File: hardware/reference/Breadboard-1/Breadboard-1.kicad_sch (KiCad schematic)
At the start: 62 parts, among them J1 Left, J2 Right, J3 ICSP, J4 TTL Serial, Q31 HSM0903, Q32 HSM0903, Q33 DTC143ZE, Q34 DTC143ZE, Q41 2N7002, Q42 2N7002, Q43 2N7002, U11 AMS1117-5.0, U21 PIC18F06Q40-x/SS

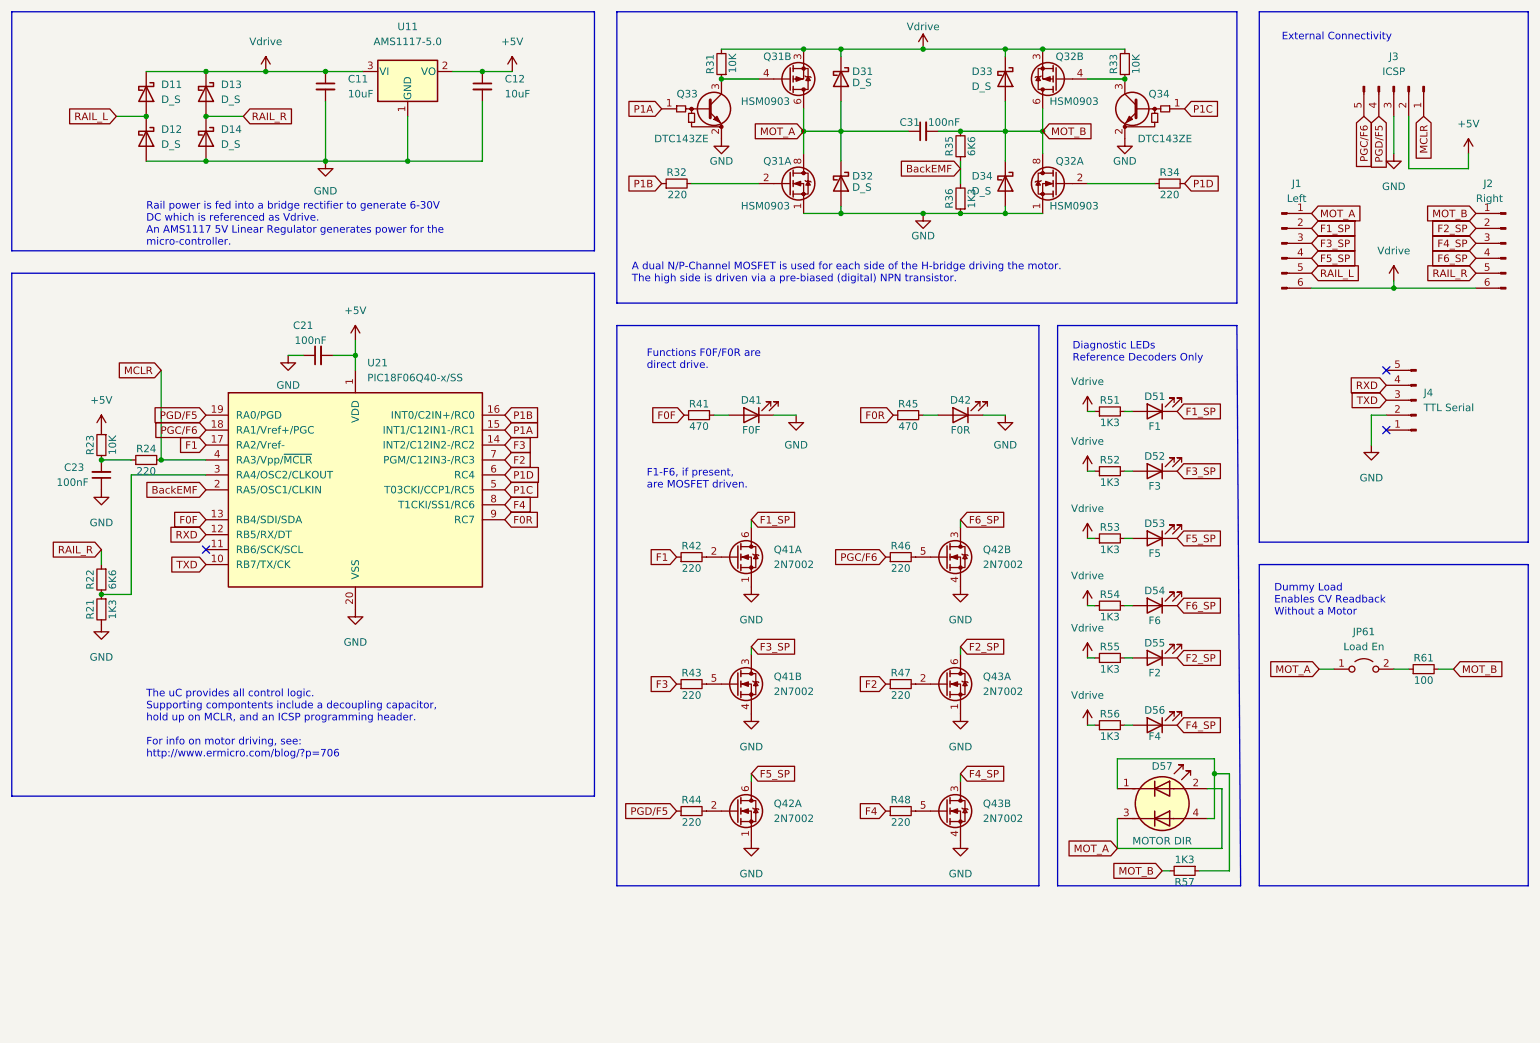
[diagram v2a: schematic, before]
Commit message: Attempt to refactor with all SOT-23 components for cost, availability.
Also makes it more possible to hand-solder.
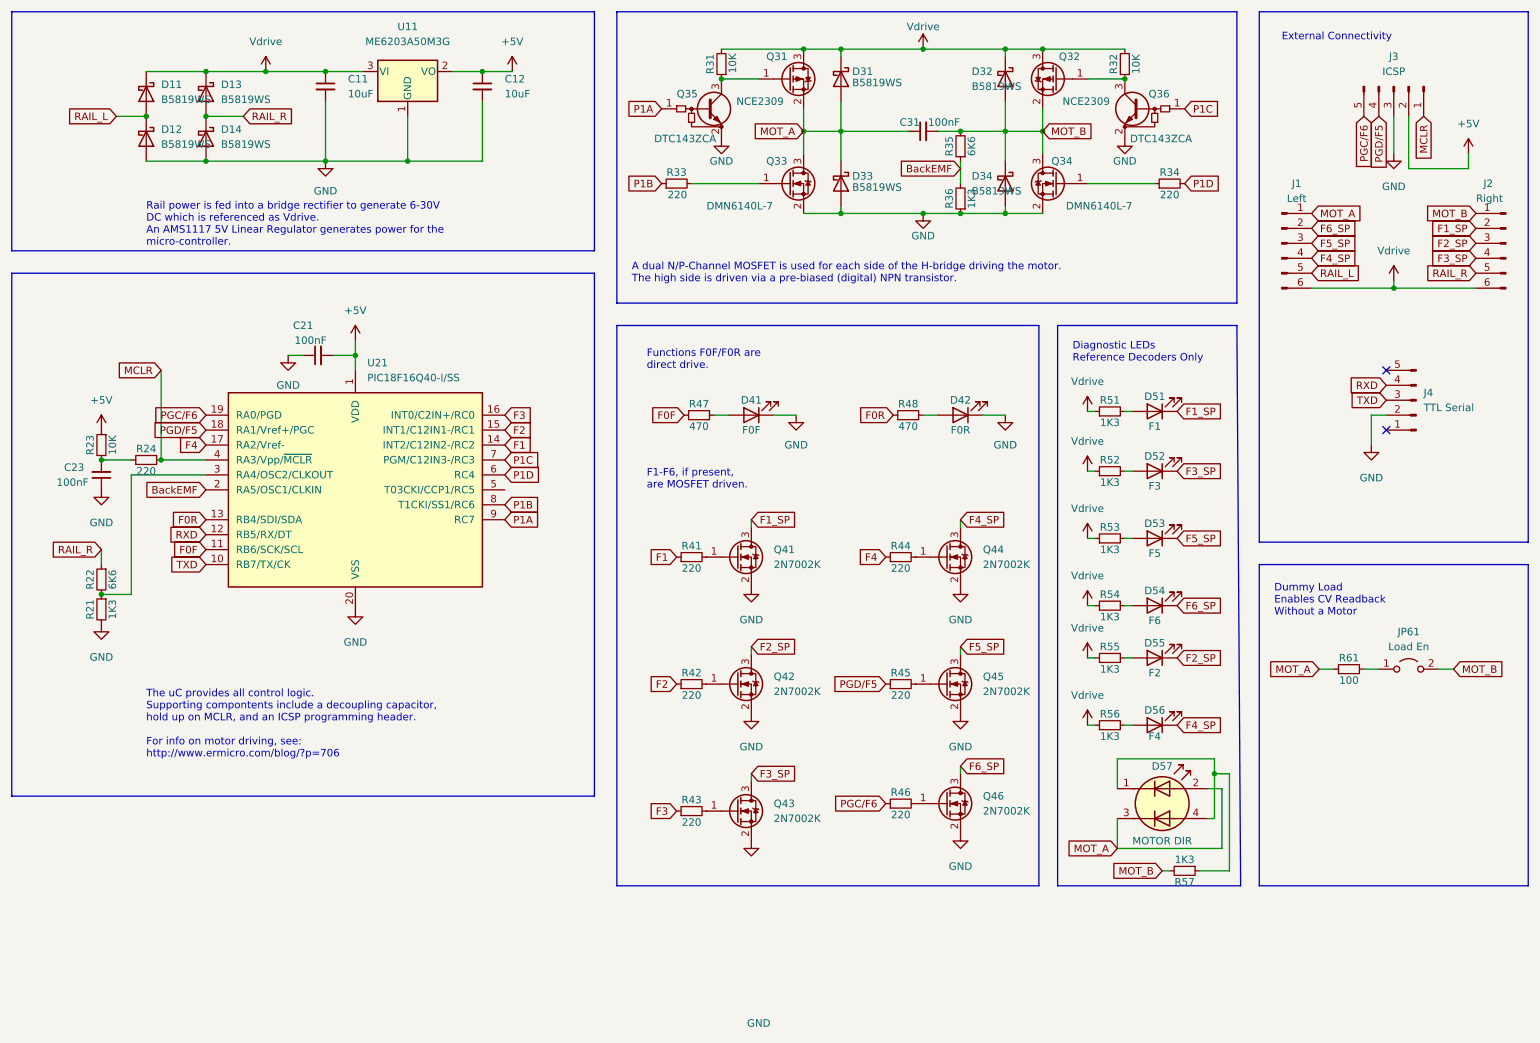
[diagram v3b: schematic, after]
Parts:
- removed Q31, Q32: HSM0903, Package_SO:SOP-8_3.9x4.9mm_P1.27mm, symbol Leo's Library:TPC8408
- removed Q41, Q42, Q43: 2N7002, Package_TO_SOT_SMD:SOT-363_SC-70-6, symbol Transistor_FET:FDG1024NZ
- added Q31, Q32: NCE2309, Package_TO_SOT_SMD:SOT-23, symbol Transistor_FET:AO3401A
- added Q33, Q34: DMN6140L-7, Package_TO_SOT_SMD:SOT-23, symbol Transistor_FET:2N7002K
- added Q41, Q42, Q43, Q44, Q45, Q46: 2N7002K, Package_TO_SOT_SMD:SOT-23, symbol Transistor_FET:2N7002K
- C11, C12: Cost (none) -> 0.10
- C21, C23, C31: footprint Capacitor_SMD:C_0402_1005Metric -> Capacitor_SMD:C_0805_2012Metric; Cost (none) -> 0.01; Specification 0402 50V 100nF X7R 10% -> 0805 50V 100nF X7R 10%
- D11, D12, D13, D14, D31, D34: value D_S -> B5819WS; footprint Diode_SMD:D_SOD-523 -> Diode_SMD:D_SOD-323; Cost (none) -> 0.01; Specification SOD-523, 50V, 1A Schottky barrier rectifier diode -> SOD-323, 40V, 1A Schottky barrier rectifier diode
- D32: renamed from D33; value D_S -> B5819WS; footprint Diode_SMD:D_SOD-523 -> Diode_SMD:D_SOD-323; Cost (none) -> 0.01; Specification SOD-523, 50V, 1A Schottky barrier rectifier diode -> SOD-323, 40V, 1A Schottky barrier rectifier diode
- D33: renamed from D32; value D_S -> B5819WS; footprint Diode_SMD:D_SOD-523 -> Diode_SMD:D_SOD-323; Cost (none) -> 0.01; Specification SOD-523, 50V, 1A Schottky barrier rectifier diode -> SOD-323, 40V, 1A Schottky barrier rectifier diode
- D41, D42, D51, D52, D53, D54, D55, D56, J1, J2: Cost (none) -> 0.02
- D57: Cost (none) -> 0.02; Specification (none) -> 1210 RG LED, 20ma, Vf 1.95v
- J3: Cost (none) -> 0.03; Specification 5 position 2.54mm pin header -> 5 position 2.54mm pin header - right angle
- J4: Cost (none) -> 0.02; Specification 5 position 2.54mm pin header -> 5 position 2.54mm pin socket
- JP61: Cost (none) -> 0.01; Specification (none) -> 2 position 2.54mm pin header
- Q35: renamed from Q33; value DTC143ZE -> DTC143ZCA; footprint Package_TO_SOT_SMD:SOT-523 -> Package_TO_SOT_SMD:SOT-23; Cost (none) -> 0.02; Specification (none) -> SOT-23 50V 100ma NPN - Pre Biased 4.7K/47K
- Q36: renamed from Q34; value DTC143ZE -> DTC143ZCA; footprint Package_TO_SOT_SMD:SOT-523 -> Package_TO_SOT_SMD:SOT-23; Cost (none) -> 0.02; Specification (none) -> SOT-23 50V 100ma NPN - Pre Biased 4.7K/47K
- R21, R36, R51, R52, R53, R54, R55, R56, R57: footprint Resistor_SMD:R_0402_1005Metric -> Resistor_SMD:R_0805_2012Metric; Cost (none) -> 0.01; Specification 0402 1.33K Ω 1% 1/8W -> 0805 1.33K Ω 1% 1/8W
- R22, R35: footprint Resistor_SMD:R_0402_1005Metric -> Resistor_SMD:R_0805_2012Metric; Cost (none) -> 0.01; Specification 0402 6.65K Ω 1% 1/8W -> 0805 6.65K Ω 1% 1/8W
- R23, R31: footprint Resistor_SMD:R_0402_1005Metric -> Resistor_SMD:R_0805_2012Metric; Cost (none) -> 0.01; Specification 0402 10K Ω 1% 1/8W -> 0805 10K Ω 1% 1/8W
- R24, R34, R43, R46: footprint Resistor_SMD:R_0402_1005Metric -> Resistor_SMD:R_0805_2012Metric; Cost (none) -> 0.01; Specification 0402 220 Ω 1% 1/8W -> 0805 220 Ω 1% 1/8W
- R32: renamed from R33; footprint Resistor_SMD:R_0402_1005Metric -> Resistor_SMD:R_0805_2012Metric; Cost (none) -> 0.01; Specification 0402 10K Ω 1% 1/8W -> 0805 10K Ω 1% 1/8W
- R33: renamed from R32; footprint Resistor_SMD:R_0402_1005Metric -> Resistor_SMD:R_0805_2012Metric; Cost (none) -> 0.01; Specification 0402 220 Ω 1% 1/8W -> 0805 220 Ω 1% 1/8W
- R41: renamed from R42; footprint Resistor_SMD:R_0402_1005Metric -> Resistor_SMD:R_0805_2012Metric; Cost (none) -> 0.01; Specification 0402 220 Ω 1% 1/8W -> 0805 220 Ω 1% 1/8W
- R42: renamed from R47; footprint Resistor_SMD:R_0402_1005Metric -> Resistor_SMD:R_0805_2012Metric; Cost (none) -> 0.01; Specification 0402 220 Ω 1% 1/8W -> 0805 220 Ω 1% 1/8W
- R44: renamed from R48; footprint Resistor_SMD:R_0402_1005Metric -> Resistor_SMD:R_0805_2012Metric; Cost (none) -> 0.01; Specification 0402 220 Ω 1% 1/8W -> 0805 220 Ω 1% 1/8W
- R45: renamed from R44; footprint Resistor_SMD:R_0402_1005Metric -> Resistor_SMD:R_0805_2012Metric; Cost (none) -> 0.01; Specification 0402 220 Ω 1% 1/8W -> 0805 220 Ω 1% 1/8W
- R47: renamed from R41; footprint Resistor_SMD:R_0402_1005Metric -> Resistor_SMD:R_0805_2012Metric; Cost (none) -> 0.01; Specification 0402 470 Ω 1% 1/8W -> 0805 470 Ω 1% 1/8W
- R48: renamed from R45; footprint Resistor_SMD:R_0402_1005Metric -> Resistor_SMD:R_0805_2012Metric; Cost (none) -> 0.01; Specification 0402 470 Ω 1% 1/8W -> 0805 470 Ω 1% 1/8W
- R61: Cost (none) -> 0.01
- U11: value AMS1117-5.0 -> ME6203A50M3G; footprint Package_TO_SOT_SMD:SOT-223-3_TabPin2 -> Package_TO_SOT_SMD:SOT-23; Cost (none) -> 0.08; Specification 5V Linear Regulator -> SOT-23 180ma 40V to 5V LDO
- U21: value PIC18F06Q40-x/SS -> PIC18F16Q40-I/SS; Cost (none) -> 1.50
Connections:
- net F0F: now also U21.11 (RB6/SCK/SCL); no longer U21.13 (RB4/SDI/SDA)
- net F0R: now also U21.13 (RB4/SDI/SDA); no longer U21.9 (RC7)
- net F1: now also U21.14 (INT2/C12IN2-/RC2); no longer U21.17 (RA2/Vref-)
- net F1_SP: now also J2.2 (Pin_2), Q41.3 (D); no longer J1.2 (Pin_2)
- net F2: now also U21.15 (INT1/C12IN1-/RC1); no longer U21.7 (PGM/C12IN3-/RC3)
- net F2_SP: now also J2.3 (Pin_3), Q42.3 (D); no longer J2.2 (Pin_2)
- net F3: now also U21.16 (INT0/C2IN+/RC0); no longer U21.14 (INT2/C12IN2-/RC2)
- net F3_SP: now also J2.4 (Pin_4), Q43.3 (D); no longer J1.3 (Pin_3)
- net F4: now also U21.17 (RA2/Vref-); no longer U21.8 (T1CKI/SS1/RC6)
- net F4_SP: now also J1.4 (Pin_4), Q44.3 (D); no longer J2.3 (Pin_3)
- net F5_SP: now also J1.3 (Pin_3), Q45.3 (D); no longer J1.4 (Pin_4)
- net F6_SP: now also J1.2 (Pin_2), Q46.3 (D); no longer J2.4 (Pin_4)
- net GND: now also Q33.2 (S), Q34.2 (S), Q41.2 (S), Q42.2 (S), Q43.2 (S), Q44.2 (S), Q45.2 (S), Q46.2 (S)
- net MOT_A: now also R61.1, Q31.2 (S), Q33.3 (D); no longer JP61.1 (A)
- net MOT_B: now also JP61.2 (B), Q32.2 (S), Q34.3 (D); no longer R61.2
- net P1A: now also U21.9 (RC7); no longer U21.15 (INT1/C12IN1-/RC1)
- net P1B: now also U21.8 (T1CKI/SS1/RC6); no longer U21.16 (INT0/C2IN+/RC0)
- net P1C: now also U21.7 (PGM/C12IN3-/RC3); no longer U21.5 (T03CKI/CCP1/RC5)
- net PGC/F6: now also U21.19 (RA0/PGD); no longer U21.18 (RA1/Vref+/PGC)
- net PGD/F5: now also U21.18 (RA1/Vref+/PGC); no longer U21.19 (RA0/PGD)
- net Vdrive: now also Q31.3 (D), Q32.3 (D)
- net at Q36.3 (C), R32.1: now also Q32.1 (G)
- net at R44.2: now also Q44.1 (G)
- net at R42.2: now also Q42.1 (G)
- net at R43.2: now also Q43.1 (G)
- net at R46.2: now also Q46.1 (G)
- net at R45.2: now also Q45.1 (G)
- net at Q35.3 (C), R31.1: now also Q31.1 (G)
- net at R33.2: now also Q33.1 (G)
- net at R34.1: now also Q34.1 (G)
- net at R41.2: now also Q41.1 (G)
- new net: JP61.1 (A), R61.2
- no-connect marks 3 -> 2
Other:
- moved on the sheet: JP61, R42, R43, R44, R45, R46, R61

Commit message: Cleanup of the final PCB.
Moved components to grid coordinates.
Added in some labels for the user.
Cleaned up some trace routing, and made it pretty where possible.
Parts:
- removed D31, D32, D33, D34: B5819WS, Diode_SMD:D_SOD-323, symbol Device:D_Schottky
- added C32: 1uF, Capacitor_SMD:C_0805_2012Metric, symbol Device:C_Small
- added J4: Oscilloscope, Connector_PinHeader_2.54mm:PinHeader_1x07_P2.54mm_Vertical, symbol Connector:Conn_01x07_Male
- added R36: 6K6, Resistor_SMD:R_0805_2012Metric, symbol Device:R_Small
- J5: renamed from J4; footprint Connector_PinSocket_2.54mm:PinSocket_1x05_P2.54mm_Vertical -> Connector_PinSocket_2.54mm:PinSocket_1x05_P2.54mm_Horizontal
- renumbered R36 to R37
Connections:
- net BackEMF: now also J4.5 (Pin_5), R36.1
- net GND: now also C31.1, J5.4 (Pin_4), C32.1, J4.7 (Pin_7); no longer J5.2 (Pin_2)
- net MOT_A: now also R35.2; no longer C31.1
- net MOT_B: now also R36.2; no longer C31.2, R35.2
- net P1A: now also J4.1 (Pin_1)
- net P1B: now also J4.2 (Pin_2)
- net P1C: now also J4.3 (Pin_3)
- net P1D: now also J4.4 (Pin_4)
- net RXD: now also J5.2 (Pin_2); no longer J5.4 (Pin_4)
- net Vdrive: now also C31.2, C32.2
- net DCC_IN: now reaches R21.1, R22.2, U21.3 (RA4/OSC2/CLKOUT)
- net DCC_IN: now also J4.6 (Pin_6)
- no-connect marks 2 -> 3
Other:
- note added: "A dual N/P-Channel MOSFET is used for each side of the H-bridge driving the motor. The high side is driven via a pre-biased (digital) NPN transistor. A trio of resistors create a single BackEMF measurement independent of motor direction."
- note removed: "A dual N/P-Channel MOSFET is used for each side of the H-bridge driving the motor. The high side is driven via a pre-biased (digital) NPN transistor."
- moved on the sheet: C23, C31, J5, R21, R22, R23, R24, R35, R37

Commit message: Minor design tweak, update documentation.
Moved the MCLEAR hold up components to make the board design cleaner.

Updated all the documentation to match the current configuration.
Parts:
- J3: Cost 0.03 -> 0.02
- J4: Cost (none) -> 0.02; Specification (none) -> 7 position 2.54mm pin header
- J5: Specification 5 position 2.54mm pin socket -> 5 position 2.54mm pin socket - right angle
- JP61: Cost 0.01 -> 0.02
- R61: Cost 0.01 -> 0.12
- U21: Specification (none) -> PIC18F16Q40-I/SS, PIC18F16Q40T-I/SS, PIC18F16Q40-E/SS
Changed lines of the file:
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@@
   (junction (at 73.66 73.66) (diameter 0) (color 0 0 0 0)
   )
+  (junction (at 154.94 35.56) (diameter 0) (color 0 0 0 0)
+  )
   (junction (at 27.94 114.3) (diameter 0) (color 0 0 0 0)
   )
@@
   )
   (junction (at 68.58 40.64) (diameter 0) (color 0 0 0 0)
+  )
+  (junction (at 185.42 35.56) (diameter 0) (color 0 0 0 0)
   )
   (junction (at 48.26 25.4) (diameter 0) (color 0 0 0 0)
@@
     (stroke (width 0) (type default) (color 0 0 0 0))
   )
+  (wire (pts (xy 154.94 35.56) (xy 160.02 35.56))
+    (stroke (width 0) (type default) (color 0 0 0 0))
+  )
   (wire (pts (xy 219.71 142.24) (xy 219.71 144.78))
     (stroke (width 0) (type default) (color 0 0 0 0))
@@
   )
   (wire (pts (xy 165.1 26.67) (xy 165.1 29.21))
+    (stroke (width 0) (type default) (color 0 0 0 0))
+  )
+  (wire (pts (xy 180.34 35.56) (xy 185.42 35.56))
     (stroke (width 0) (type default) (color 0 0 0 0))
   )
@@
     )
   )
-  (global_label "MOT_B" (shape input) (at 190.5 35.56 0) (fields_autoplaced)
-    (effects (font (size 1.27 1.27)) (justify left))
-    (property "Intersheet References" "${INTERSHEET_REFS}" (id 0) (at 198.9002 35.4806 0)
-      (effects (font (size 1.27 1.27)) (justify left) hide)
+  (global_label "MOT_B" (shape input) (at 180.34 35.56 180) (fields_autoplaced)
+    (effects (font (size 1.27 1.27)) (justify right))
+    (property "Intersheet References" "${INTERSHEET_REFS}" (id 0) (at 171.9398 35.6394 0)
+      (effects (font (size 1.27 1.27)) (justify right) hide)
     )
   )
@@
     )
   )
-  (global_label "MOT_A" (shape input) (at 149.86 35.56 180) (fields_autoplaced)
-    (effects (font (size 1.27 1.27)) (justify right))
-    (property "Intersheet References" "${INTERSHEET_REFS}" (id 0) (at 141.6412 35.4806 0)
-      (effects (font (size 1.27 1.27)) (justify right) hide)
+  (global_label "MOT_A" (shape input) (at 160.02 35.56 0) (fields_autoplaced)
+    (effects (font (size 1.27 1.27)) (justify left))
+    (property "Intersheet References" "${INTERSHEET_REFS}" (id 0) (at 168.2388 35.6394 0)
+      (effects (font (size 1.27 1.27)) (justify left) hide)
     )
   )
@@
       (effects (font (size 1.27 1.27)) hide)
     )
-    (property "Cost" "0.01" (id 5) (at 242.57 127 0)
+    (property "Cost" "0.12" (id 5) (at 242.57 127 0)
       (effects (font (size 1.27 1.27)) hide)
     )
@@
     )
     (property "Cost" "1.50" (id 4) (at 73.66 96.52 0)
+      (effects (font (size 1.27 1.27)) hide)
+    )
+    (property "Specification" "PIC18F16Q40-I/SS, PIC18F16Q40T-I/SS, PIC18F16Q40-E/SS" (id 5) (at 73.66 96.52 0)
       (effects (font (size 1.27 1.27)) hide)
     )
@@
       (effects (font (size 1.27 1.27)) hide)
     )
-    (property "Cost" "0.01" (id 5) (at 252.73 127 0)
+    (property "Cost" "0.02" (id 5) (at 252.73 127 0)
       (effects (font (size 1.27 1.27)) hide)
     )
@@
       (effects (font (size 1.27 1.27)) hide)
     )
-    (property "Specification" "5 position 2.54mm pin socket" (id 4) (at 267.97 78.74 0)
+    (property "Specification" "5 position 2.54mm pin socket - right angle" (id 4) (at 267.97 78.74 0)
       (effects (font (size 1.27 1.27)) hide)
     )
@@
       (effects (font (size 1.27 1.27)) hide)
     )
-    (property "Datasheet" "~" (id 3) (at 231.14 81.28 0)
+    (property "Datasheet" "Generic Passive" (id 3) (at 231.14 81.28 0)
+      (effects (font (size 1.27 1.27)) hide)
+    )
+    (property "Cost" "0.02" (id 4) (at 231.14 81.28 0)
+      (effects (font (size 1.27 1.27)) hide)
+    )
+    (property "Specification" "7 position 2.54mm pin header" (id 5) (at 231.14 81.28 0)
       (effects (font (size 1.27 1.27)) hide)
     )
@@
       (effects (font (size 1.27 1.27)) hide)
     )
-    (property "Cost" "0.03" (id 5) (at 250.19 27.94 0)
-      (effects (font (size 1.27 1.27)) hide)
-    )
+    (property "Cost" "0.02" (id 5) (at 250.19 27.94 0)
+      (effects (font (size 1.27 1.27)) hide)
+    )

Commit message: Manufacturability changes.
Added 3 fiducial markers to support pick and place in volume.
Resized all the traces to be manufacturable with the popular board fabs.
Moved traces based on the new size.
Standardized vias to one size larger than the general manufacturing minimum.
Improved grounding around the CPU.
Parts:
- added FID1, FID2, FID3: Fiducial, Fiducial:Fiducial_0.75mm_Mask2.25mm, symbol Mechanical:Fiducial
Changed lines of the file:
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@@
     (pin "3")
+  )
+  (symbol (lib_id "Mechanical:Fiducial") (at 101.6 132.08 0) (unit 1)
+    (in_bom yes) (on_board yes) (fields_autoplaced)
+    (property "Reference" "FID3" (id 0) (at 104.14 130.8099 0)
+      (effects (font (size 1.27 1.27)) (justify left))
+    )
+    (property "Value" "Fiducial" (id 1) (at 104.14 133.3499 0)
+      (effects (font (size 1.27 1.27)) (justify left))
+    )
+    (property "Footprint" "Fiducial:Fiducial_0.75mm_Mask2.25mm" (id 2) (at 101.6 132.08 0)
+      (effects (font (size 1.27 1.27)) hide)
+    )
+    (property "Datasheet" "~" (id 3) (at 101.6 132.08 0)
+      (effects (font (size 1.27 1.27)) hide)
+    )
   )
   (symbol (lib_id "power:Vdrive") (at 198.12 104.775 0) (unit 1)
@@
     (pin "2")
   )
+  (symbol (lib_id "Mechanical:Fiducial") (at 101.6 125.73 0) (unit 1)
+    (in_bom yes) (on_board yes) (fields_autoplaced)
+    (property "Reference" "FID2" (id 0) (at 104.14 124.4599 0)
+      (effects (font (size 1.27 1.27)) (justify left))
+    )
+    (property "Value" "Fiducial" (id 1) (at 104.14 126.9999 0)
+      (effects (font (size 1.27 1.27)) (justify left))
+    )
+    (property "Footprint" "Fiducial:Fiducial_0.75mm_Mask2.25mm" (id 2) (at 101.6 125.73 0)
+      (effects (font (size 1.27 1.27)) hide)
+    )
+    (property "Datasheet" "~" (id 3) (at 101.6 125.73 0)
+      (effects (font (size 1.27 1.27)) hide)
+    )
+  )
   (symbol (lib_id "power:GND") (at 170.18 29.21 0) (unit 1)
     (in_bom yes) (on_board yes)
@@
     (pin "2")
     (pin "3")
+  )
+  (symbol (lib_id "Mechanical:Fiducial") (at 101.6 119.38 0) (unit 1)
+    (in_bom yes) (on_board yes) (fields_autoplaced)
+    (property "Reference" "FID1" (id 0) (at 104.14 118.1099 0)
+      (effects (font (size 1.27 1.27)) (justify left))
+    )
+    (property "Value" "Fiducial" (id 1) (at 104.14 120.6499 0)
+      (effects (font (size 1.27 1.27)) (justify left))
+    )
+    (property "Footprint" "Fiducial:Fiducial_0.75mm_Mask2.25mm" (id 2) (at 101.6 119.38 0)
+      (effects (font (size 1.27 1.27)) hide)
+    )
+    (property "Datasheet" "~" (id 3) (at 101.6 119.38 0)
+      (effects (font (size 1.27 1.27)) hide)
+    )
   )
   (symbol (lib_id "power:+5V") (at 100.33 25.4 0) (unit 1)
@@
       (reference "D57") (unit 1) (value "MOTOR DIR") (footprint "LED_SMD:LED_RGB_1210")
     )
+    (path "/b1e3d7d1-5e1a-4783-b95d-60ad9975723b"
+      (reference "FID1") (unit 1) (value "Fiducial") (footprint "Fiducial:Fiducial_0.75mm_Mask2.25mm")
+    )
+    (path "/89d0e1b6-392a-4bac-b2c2-159e11a37d08"
+      (reference "FID2") (unit 1) (value "Fiducial") (footprint "Fiducial:Fiducial_0.75mm_Mask2.25mm")
+    )
+    (path "/1559fcdf-2609-4899-b549-fce5da783422"
+      (reference "FID3") (unit 1) (value "Fiducial") (footprint "Fiducial:Fiducial_0.75mm_Mask2.25mm")
+    )
     (path "/84e5506c-143e-495f-9aa4-d3a71622f213"
